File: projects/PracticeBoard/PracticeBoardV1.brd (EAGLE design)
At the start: 160 x 100 mm, 12 parts, among them U1 TPS63001

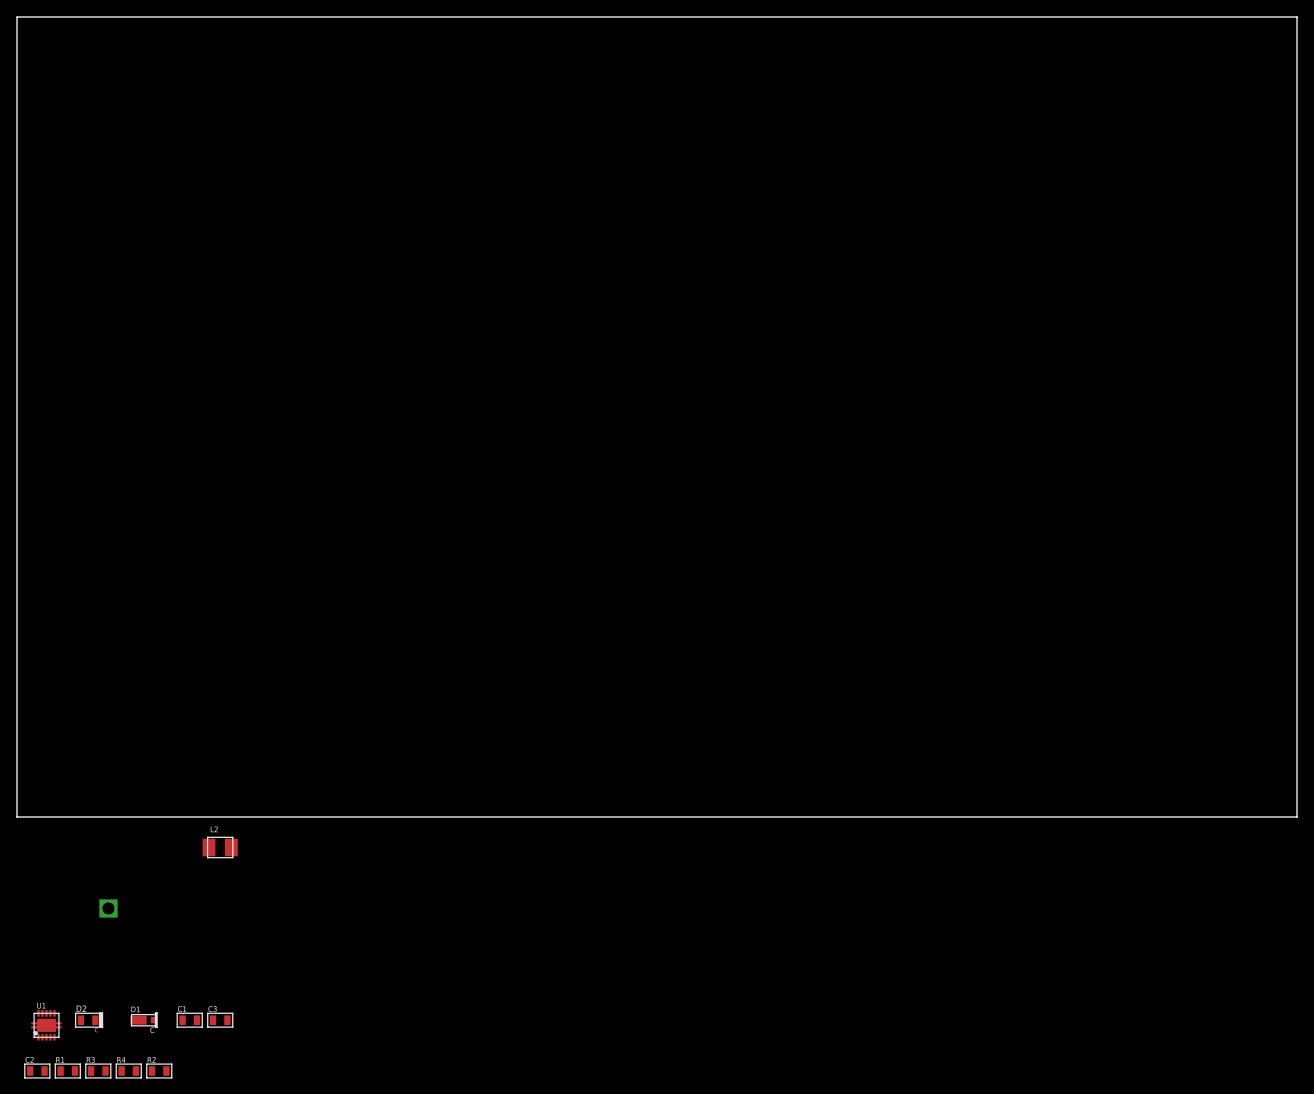
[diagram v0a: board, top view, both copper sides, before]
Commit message: Added the SN74LV04A-Hex-Inverter and corresponding package 14-TSSOP to BSE lib
>  Also worked on prepping the PracticeBoardV1 board a tiny bit
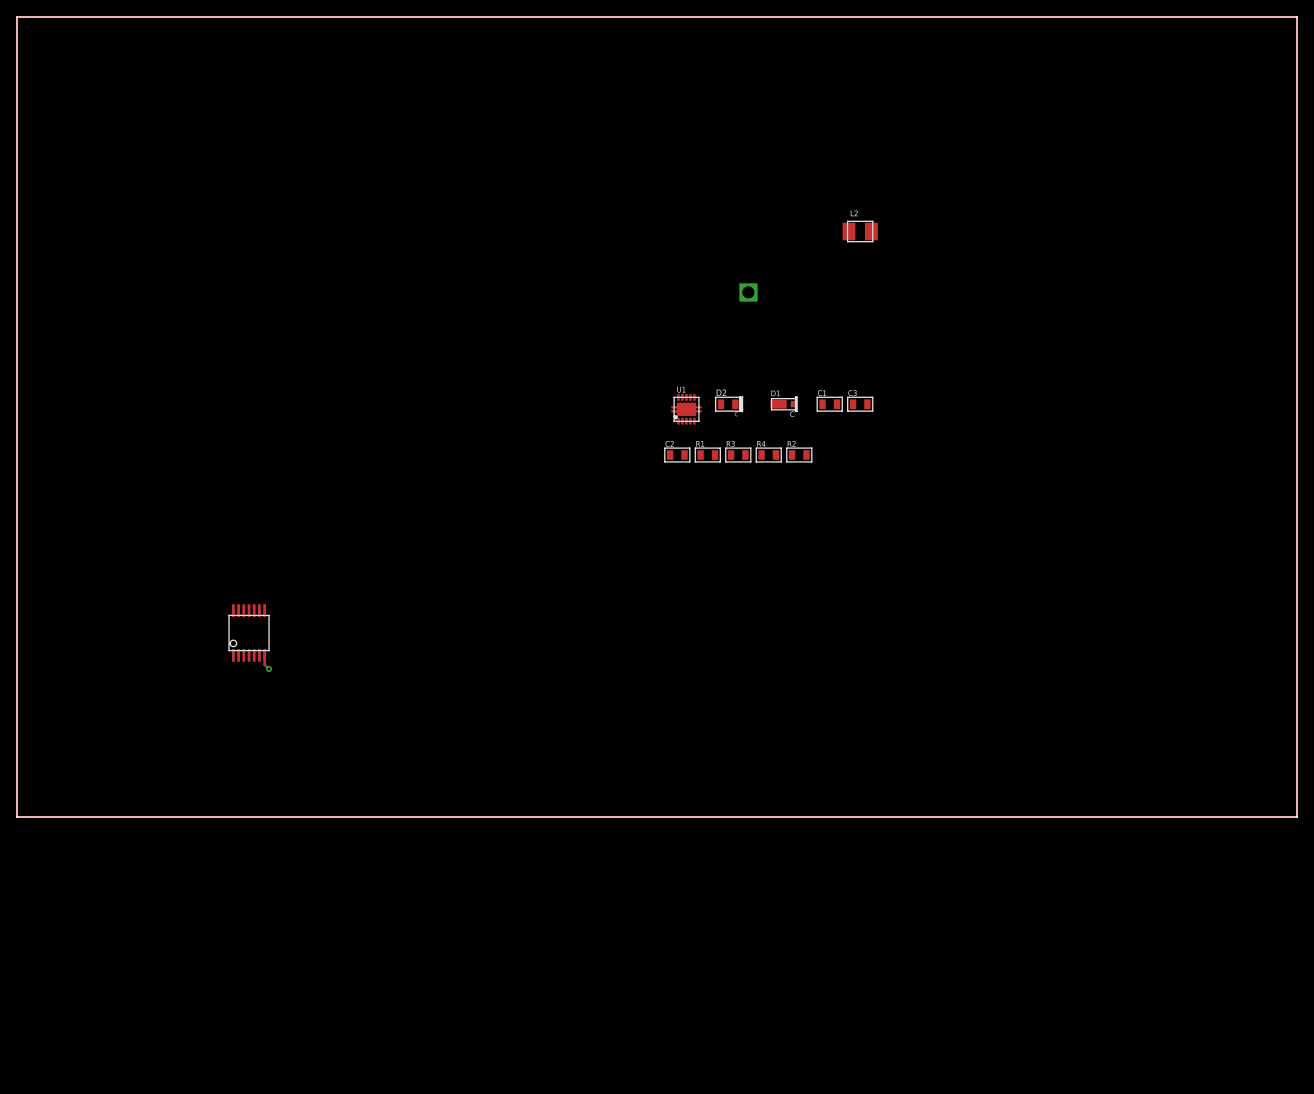
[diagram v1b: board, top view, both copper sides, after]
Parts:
- added U2: (no value), BrownSpaceEngineering:14-TSSOP
- V1: value 3V3 -> +3V3
- moved C1 111.0 mm to (101.6, 51.6)
- moved C2 111.0 mm to (82.5, 45.2)
- moved C3 111.0 mm to (105.4, 51.6)
- moved D1 111.0 mm to (96.5, 51.6)
- moved D2 111.0 mm to (88.9, 51.6)
- moved L2 111.0 mm to (105.4, 73.2)
- moved R1 111.0 mm to (86.3, 45.2)
- moved R2 111.0 mm to (97.8, 45.2)
- moved R3 111.0 mm to (90.2, 45.2)
- moved R4 111.0 mm to (94.0, 45.2)
- moved U1 111.0 mm to (82.5, 49.1)
- moved V1 111.0 mm to (91.4, 65.6)
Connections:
- net +3V3: now also U2.P14
- net GND: now also U2.P7
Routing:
- net DIM-WIRE: track 0.00 -> 520.0 mm
- net GND: track 0.00 -> 1.93 mm, vias 0 -> 1
- added copper zone on layer 1, net +3V3
- added copper zone on layer 16, net GND

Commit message: Added coin battery holder to lib; Added astable timer and AND/OR led circuit to PracticeBoardV1
Still need the LED enable circuit from ControlBoard ???
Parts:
- added BATTERY: BC-2003-COIN-BATTERY-HOLDER, BrownSpaceEngineering:BC-2003-COIN-BATTERY-HOLDER
- added C4: 0.01uF, BrownSpaceEngineering:0805
- added C5, R7: (no value), BrownSpaceEngineering:0805
- added D3, D4, D5: LED0805, BrownSpaceEngineering:0805-D
- added POTENTIOMETER-IN, POTENTIOMETER-OUT: (no value), BrownSpaceEngineering:VIA-60MIL-SQ
- added R5: (no value), BrownSpaceEngineering:1210
- added U3: SNX4AHC08-QUAD-2IN-AND, BrownSpaceEngineering:VQFN-14
- added U4: SN74LV32A-QUAD-2IN-OR, BrownSpaceEngineering:TSSOP-14
- added V2: OUT1, BrownSpaceEngineering:VIA-60MIL-SQ
- added V3: IN2, BrownSpaceEngineering:VIA-60MIL-SQ
- added V4: OUT2, BrownSpaceEngineering:VIA-60MIL-SQ
- added V5: IN1, BrownSpaceEngineering:VIA-60MIL-SQ
- added V6: IN3, BrownSpaceEngineering:VIA-60MIL-SQ
- added V7: OUT3, BrownSpaceEngineering:VIA-60MIL-SQ
- U2: device BrownSpaceEngineering:14-TSSOP -> BrownSpaceEngineering:SO-8
- moved U2 48.2 mm to (-3.00, -13.0)
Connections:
- new net N$1: D3.A, U2.P$3
- new net N$10: U3.P3, U3.P4
- new net N$11: U3.P5, U4.P5, V7.P$1
- new net N$12: D4.A, U3.P6
- new net N$13: U4.P3, U4.P4
- new net N$14: D5.A, U4.P6
- new net N$2: C4.1, U2.P$5
- new net N$3: C5.1, POTENTIOMETER-IN.P$1, U2.P$2, U2.P$6
- new net N$4: U3.P1, U4.P1, V2.P$1
- new net N$7: POTENTIOMETER-OUT.P$1, R7.1, U2.P$7
- new net N$8: U3.P2, U4.P2, V4.P$1
- net +3V3: now also R7.2, U2.P$4, U2.P$8, U3.P14, U4.P14, V3.P$1, V5.P$1, V6.P$1; no longer U2.P14
- net GND: now also BATTERY.-, C4.2, C5.2, D3.C, D4.C, D5.C, U2.P$1, U3.P7, U4.P7; no longer U2.P7
- net VIN: now also BATTERY.+(1), BATTERY.+(2)
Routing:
- net GND: track 1.93 -> 0.00 mm, vias 1 -> 0
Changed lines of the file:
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@@
 <element name="R2" library="BrownSpaceEngineering" package="0805" value="330R" x="97.78" y="45.25"/>
 <element name="V1" library="BrownSpaceEngineering" package="VIA-60MIL-SQ" value="+3V3" x="91.43" y="65.57"/>
-<element name="U2" library="BrownSpaceEngineering" package="14-TSSOP" value="" x="29" y="23"/>
+<element name="BATTERY" library="BrownSpaceEngineering" package="BC-2003-COIN-BATTERY-HOLDER" value="BC-2003-COIN-BATTERY-HOLDER" x="14" y="-10"/>
+<element name="U2" library="BrownSpaceEngineering" package="SO-8" value="" x="-3" y="-13"/>
+<element name="R7" library="BrownSpaceEngineering" package="0805" value="" x="-4" y="-32"/>
+<element name="C4" library="BrownSpaceEngineering" package="0805" value="0.01uF" x="-4" y="-42"/>
+<element name="C5" library="BrownSpaceEngineering" package="0805" value="" x="-4" y="-47"/>
+<element name="D3" library="BrownSpaceEngineering" package="0805-D" value="LED0805" x="-4" y="-52"/>
+<element name="POTENTIOMETER-IN" library="BrownSpaceEngineering" package="VIA-60MIL-SQ" value="" x="5" y="-89"/>
+<element name="POTENTIOMETER-OUT" library="BrownSpaceEngineering" package="VIA-60MIL-SQ" value="" x="5" y="-112"/>
+<element name="U3" library="BrownSpaceEngineering" package="VQFN-14" value="SNX4AHC08-QUAD-2IN-AND" x="-3" y="-127"/>
+<element name="U4" library="BrownSpaceEngineering" package="TSSOP-14" value="SN74LV32A-QUAD-2IN-OR" x="-10" y="-125"/>
+<element name="V5" library="BrownSpaceEngineering" package="VIA-60MIL-SQ" value="IN1" x="-3" y="-142"/>
+<element name="V2" library="BrownSpaceEngineering" package="VIA-60MIL-SQ" value="OUT1" x="-3" y="-165"/>
+<element name="V3" library="BrownSpaceEngineering" package="VIA-60MIL-SQ" value="IN2" x="-3" y="-188"/>
+<element name="V4" library="BrownSpaceEngineering" package="VIA-60MIL-SQ" value="OUT2" x="-3" y="-211"/>
+<element name="V6" library="BrownSpaceEngineering" package="VIA-60MIL-SQ" value="IN3" x="-3" y="-234"/>
+<element name="V7" library="BrownSpaceEngineering" package="VIA-60MIL-SQ" value="OUT3" x="-3" y="-257"/>
+<element name="D4" library="BrownSpaceEngineering" package="0805-D" value="LED0805" x="-12" y="-271"/>
+<element name="D5" library="BrownSpaceEngineering" package="0805-D" value="LED0805" x="-12" y="-276"/>
+<element name="R5" library="BrownSpaceEngineering" package="1210" value="" x="-18" y="-273"/>
 </elements>
 <signals>
@@
 <contactref element="R2" pad="2"/>
 <contactref element="V1" pad="P$1"/>
-<contactref element="U2" pad="P14"/>
 <polygon width="0.508" layer="1">
 <vertex x="0" y="0"/>
@@
 <vertex x="160" y="0"/>
 </polygon>
-<wire x1="82.679953125" y1="49.3005375" x2="82.679190625" y2="52.61803125" width="0" layer="19" extent="1-1"/>
+<contactref element="R7" pad="2"/>
+<contactref element="U2" pad="P$8"/>
+<contactref element="U2" pad="P$4"/>
+<contactref element="V5" pad="P$1"/>
+<contactref element="V3" pad="P$1"/>
+<contactref element="V6" pad="P$1"/>
+<contactref element="U3" pad="P14"/>
+<contactref element="U4" pad="P14"/>
+<wire x1="-3" y1="-188" x2="-3" y2="-234" width="0" layer="19" extent="1-1"/>
+<wire x1="-3" y1="-142" x2="-3" y2="-188" width="0" layer="19" extent="1-1"/>
+<wire x1="-4.725" y1="-127.75" x2="-3" y2="-142" width="0" layer="19" extent="1-1"/>
+<wire x1="-11.95" y1="-122.2" x2="-4.725" y2="-127.75" width="0" layer="19" extent="1-1"/>
+<wire x1="-3.1" y1="-32" x2="-11.95" y2="-122.2" width="0" layer="19" extent="1-1"/>
+<wire x1="-1.095" y1="-15.9" x2="-3.1" y2="-32" width="0" layer="19" extent="1-1"/>
+<wire x1="-4.905" y1="-10.1" x2="-1.095" y2="-15.9" width="0" layer="19" extent="1-1"/>
+<wire x1="82.679953125" y1="49.3005375" x2="-4.905" y2="-10.1" width="0" layer="19" extent="1-1"/>
+<wire x1="82.679190625" y1="52.61803125" x2="82.679953125" y2="49.3005375" width="0" layer="19" extent="1-1"/>
 <wire x1="89.26" y1="45.25" x2="82.679953125" y2="49.3005375" width="0" layer="19" extent="1-1"/>
+<wire x1="98.68" y1="45.25" x2="89.26" y2="45.25" width="0" layer="19" extent="1-1"/>
+<wire x1="97.11" y1="51.6" x2="98.68" y2="45.25" width="0" layer="19" extent="1-1"/>
+<wire x1="104.5" y1="51.6" x2="97.11" y2="51.6" width="0" layer="19" extent="1-1"/>
+<wire x1="91.43" y1="65.57" x2="97.11" y2="51.6" width="0" layer="19" extent="1-1"/>
 </signal>
 <signal name="VIN">
@@
 <contactref element="C1" pad="1"/>
 <contactref element="R1" pad="2"/>
+<contactref element="BATTERY" pad="+(1)"/>
+<contactref element="BATTERY" pad="+(2)"/>
 <wire x1="87.25" y1="45.25" x2="100.69" y2="51.6" width="0" layer="19" extent="1-1"/>
 <wire x1="84.67868125" y1="49.301809375" x2="87.25" y2="45.25" width="0" layer="19" extent="1-1"/>
+<wire x1="25.905" y1="-10" x2="87.25" y2="45.25" width="0" layer="19" extent="1-1"/>
+<wire x1="2.095" y1="-10" x2="25.905" y2="-10" width="0" layer="19" extent="1-1"/>
 </signal>
 <signal name="N$9">
@@
 <vertex x="160" y="0"/>
 </polygon>
-<contactref element="U2" pad="P7"/>
-<wire x1="30.95" y1="20.2" x2="30.95" y2="19.05" width="0.3048" layer="1"/>
-<wire x1="30.95" y1="19.05" x2="31.5" y2="18.5" width="0.3048" layer="1"/>
-<via x="31.5" y="18.5" extent="1-16" drill="0.35"/>
+<contactref element="BATTERY" pad="-"/>
+<contactref element="U2" pad="P$1"/>
+<contactref element="C4" pad="2"/>
+<contactref element="C5" pad="2"/>
+<contactref element="D3" pad="C"/>
+<contactref element="U4" pad="P7"/>
+<contactref element="D5" pad="C"/>
+<contactref element="D4" pad="C"/>
+<contactref element="U3" pad="P7"/>
 <wire x1="102.49" y1="51.6" x2="106.3" y2="51.6" width="0" layer="19" extent="1-1"/>
 <wire x1="95.21" y1="51.6" x2="102.49" y2="51.6" width="0" layer="19" extent="1-1"/>
@@
 <wire x1="83.44" y1="45.25" x2="83.681475" y2="49.301809375" width="0" layer="19" extent="1-1"/>
 <wire x1="93.07" y1="45.25" x2="95.21" y2="51.6" width="0" layer="19" extent="1-1"/>
-<wire x1="30.95" y1="20.2" x2="83.44" y2="45.25" width="0" layer="19" extent="1-1"/>
+<wire x1="14" y1="-10" x2="83.44" y2="45.25" width="0" layer="19" extent="1-1"/>
+<wire x1="-4.905" y1="-15.9" x2="14" y2="-10" width="0" layer="19" extent="1-1"/>
+<wire x1="-3.1" y1="-42" x2="-4.905" y2="-15.9" width="0" layer="19" extent="1-1"/>
+<wire x1="-3.1" y1="-47" x2="-3.1" y2="-42" width="0" layer="19" extent="1-1"/>
+<wire x1="-3.1" y1="-52" x2="-3.1" y2="-47" width="0" layer="19" extent="1-1"/>
+<wire x1="-1.275" y1="-126.25" x2="-3.1" y2="-52" width="0" layer="19" extent="1-1"/>
+<wire x1="-8.05" y1="-127.8" x2="-1.275" y2="-126.25" width="0" layer="19" extent="1-1"/>
+<wire x1="-11.1" y1="-271" x2="-8.05" y2="-127.8" width="0" layer="19" extent="1-1"/>
+<wire x1="-11.1" y1="-276" x2="-11.1" y2="-271" width="0" layer="19" extent="1-1"/>
 </signal>
 <signal name="3V3REF">
@@
 <wire x1="160" y1="0" x2="0" y2="0" width="0.254" layer="1"/>
 </signal>
+<signal name="N$2">
+<contactref element="C4" pad="1"/>
+<contactref element="U2" pad="P$5"/>
+<wire x1="-1.095" y1="-10.1" x2="-4.9" y2="-42" width="0" layer="19" extent="1-1"/>
+</signal>
+<signal name="N$7">
+<contactref element="R7" pad="1"/>
+<contactref element="U2" pad="P$7"/>
+<contactref element="POTENTIOMETER-OUT" pad="P$1"/>
+<wire x1="-4.9" y1="-32" x2="5" y2="-112" width="0" layer="19" extent="1-1"/>
+<wire x1="-3.635" y1="-10.1" x2="-4.9" y2="-32" width="0" layer="19" extent="1-1"/>
+</signal>
+<signal name="N$3">
+<contactref element="C5" pad="1"/>
+<contactref element="U2" pad="P$2"/>
+<contactref element="POTENTIOMETER-IN" pad="P$1"/>
+<contactref element="U2" pad="P$6"/>
+<wire x1="-4.9" y1="-47" x2="5" y2="-89" width="0" layer="19" extent="1-1"/>
+<wire x1="-3.635" y1="-15.9" x2="-4.9" y2="-47" width="0" layer="19" extent="1-1"/>
+<wire x1="-2.365" y1="-10.1" x2="-3.635" y2="-15.9" width="0" layer="19" extent="1-1"/>
+</signal>
+<signal name="N$1">
+<contactref element="D3" pad="A"/>
+<contactref element="U2" pad="P$3"/>
+<wire x1="-2.365" y1="-15.9" x2="-4.9" y2="-52" width="0" layer="19" extent="1-1"/>
+</signal>
+<signal name="N$4">
+<contactref element="V2" pad="P$1"/>
+<contactref element="U3" pad="P1"/>
+<contactref element="U4" pad="P1"/>
+<wire x1="-11.95" y1="-127.8" x2="-3" y2="-165" width="0" layer="19" extent="1-1"/>
+<wire x1="-4.725" y1="-126.25" x2="-11.95" y2="-127.8" width="0" layer="19" extent="1-1"/>
+</signal>
+<signal name="N$8">
+<contactref element="V4" pad="P$1"/>
+<contactref element="U3" pad="P2"/>
+<contactref element="U4" pad="P2"/>
+<wire x1="-11.3" y1="-127.8" x2="-3" y2="-211" width="0" layer="19" extent="1-1"/>
+<wire x1="-4" y1="-125.275" x2="-11.3" y2="-127.8" width="0" layer="19" extent="1-1"/>
+</signal>
+<signal name="N$10">
+<contactref element="U3" pad="P3"/>
+<contactref element="U3" pad="P4"/>
+<wire x1="-3" y1="-125.275" x2="-3.5" y2="-125.275" width="0" layer="19" extent="1-1"/>
+</signal>
+<signal name="N$11">
+<contactref element="V7" pad="P$1"/>
+<contactref element="U3" pad="P5"/>
+<contactref element="U4" pad="P5"/>
+<wire x1="-2.5" y1="-125.275" x2="-9.35" y2="-127.8" width="0" layer="19" extent="1-1"/>
+<wire x1="-3" y1="-257" x2="-9.35" y2="-127.8" width="0" layer="19" extent="1-1"/>
+</signal>
+<signal name="N$12">
+<contactref element="U3" pad="P6"/>
+<contactref element="D4" pad="A"/>
+<wire x1="-12.9" y1="-271" x2="-2" y2="-125.275" width="0" layer="19" extent="1-1"/>
+</signal>
+<signal name="N$13">
+<contactref element="U4" pad="P3"/>
+<contactref element="U4" pad="P4"/>
+<wire x1="-10" y1="-127.8" x2="-10.65" y2="-127.8" width="0" layer="19" extent="1-1"/>
+</signal>
+<signal name="N$14">
+<contactref element="U4" pad="P6"/>
+<contactref element="D5" pad="A"/>
+<wire x1="-12.9" y1="-276" x2="-8.7" y2="-127.8" width="0" layer="19" extent="1-1"/>
+</signal>
 </signals>
